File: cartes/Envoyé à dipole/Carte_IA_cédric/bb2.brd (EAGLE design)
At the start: 100 x 80 mm, 29 parts, among them IC1 MIC5219BM5

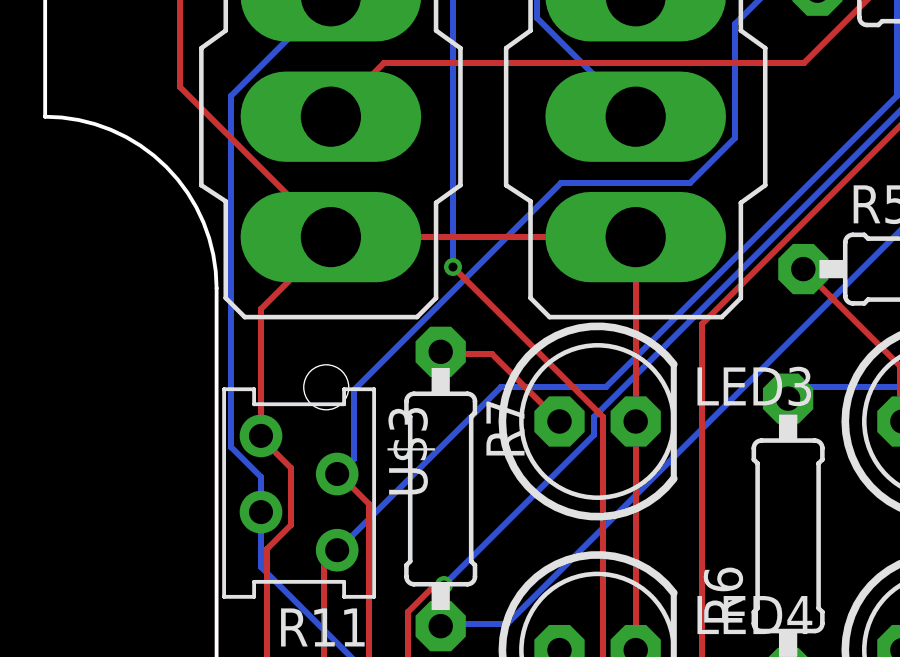
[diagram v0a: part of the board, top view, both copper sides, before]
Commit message: nouvelle version carte IA
correction bug piste trop près du détrompeur
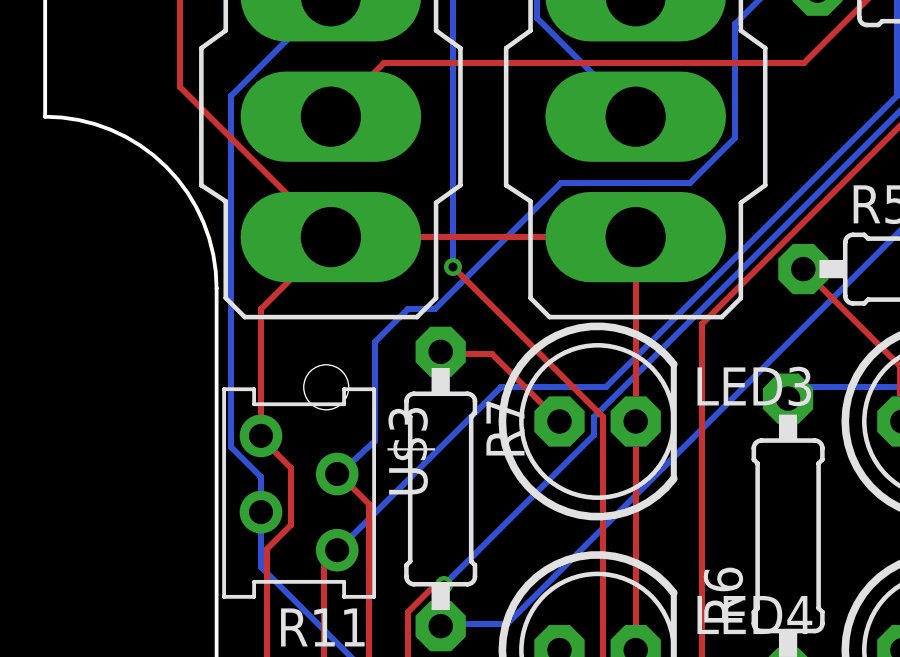
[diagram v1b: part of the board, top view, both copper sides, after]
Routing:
- net TIRETTE: track 44.9 -> 45.5 mm
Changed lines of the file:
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@@
 <wire x1="36.1" y1="65.1" x2="37.6" y2="66.6" width="0.2" layer="16"/>
 <wire x1="31.8" y1="65.1" x2="36.1" y2="65.1" width="0.2" layer="16"/>
-<wire x1="24.9" y1="58.2" x2="31.8" y2="65.1" width="0.2" layer="16"/>
-<wire x1="24.9" y1="55.9" x2="24.9" y2="58.2" width="0.2" layer="16"/>
-<wire x1="24.4" y1="55.4" x2="24.9" y2="55.9" width="0.2" layer="16"/>
+<wire x1="25.6" y1="59.8" x2="26.7" y2="60.9" width="0.2" layer="16"/>
+<wire x1="26.7" y1="60.9" x2="27.6" y2="60.9" width="0.2" layer="16"/>
+<wire x1="27.6" y1="60.9" x2="31.8" y2="65.1" width="0.2" layer="16"/>
+<wire x1="25.6" y1="56.5" x2="25.6" y2="59.8" width="0.2" layer="16"/>
+<wire x1="24.4" y1="55.4" x2="25.6" y2="56.5" width="0.2" layer="16"/>
 <wire x1="41.9" y1="78.1" x2="41.91" y2="78.105" width="0.2" layer="16"/>
 <wire x1="24.4" y1="55.4" x2="24.34" y2="55.4" width="0.2" layer="16"/>
